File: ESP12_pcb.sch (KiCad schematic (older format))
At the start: 15 parts

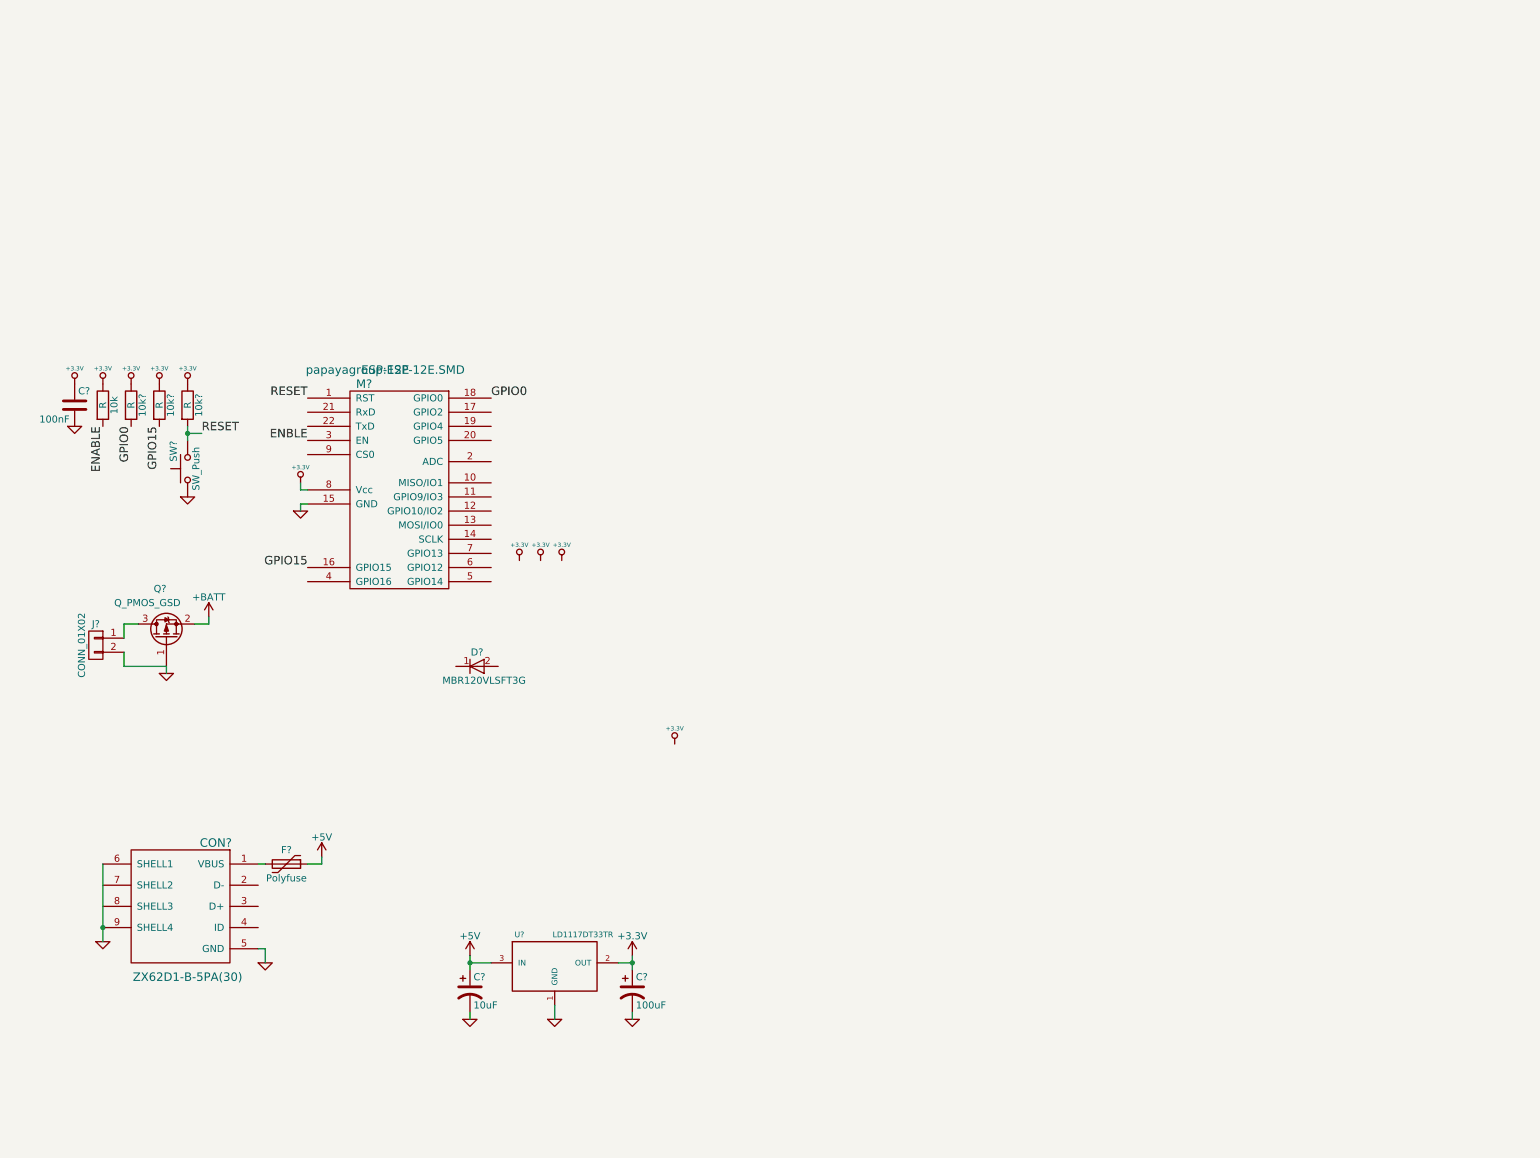
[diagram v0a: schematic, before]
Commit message: Finished power components
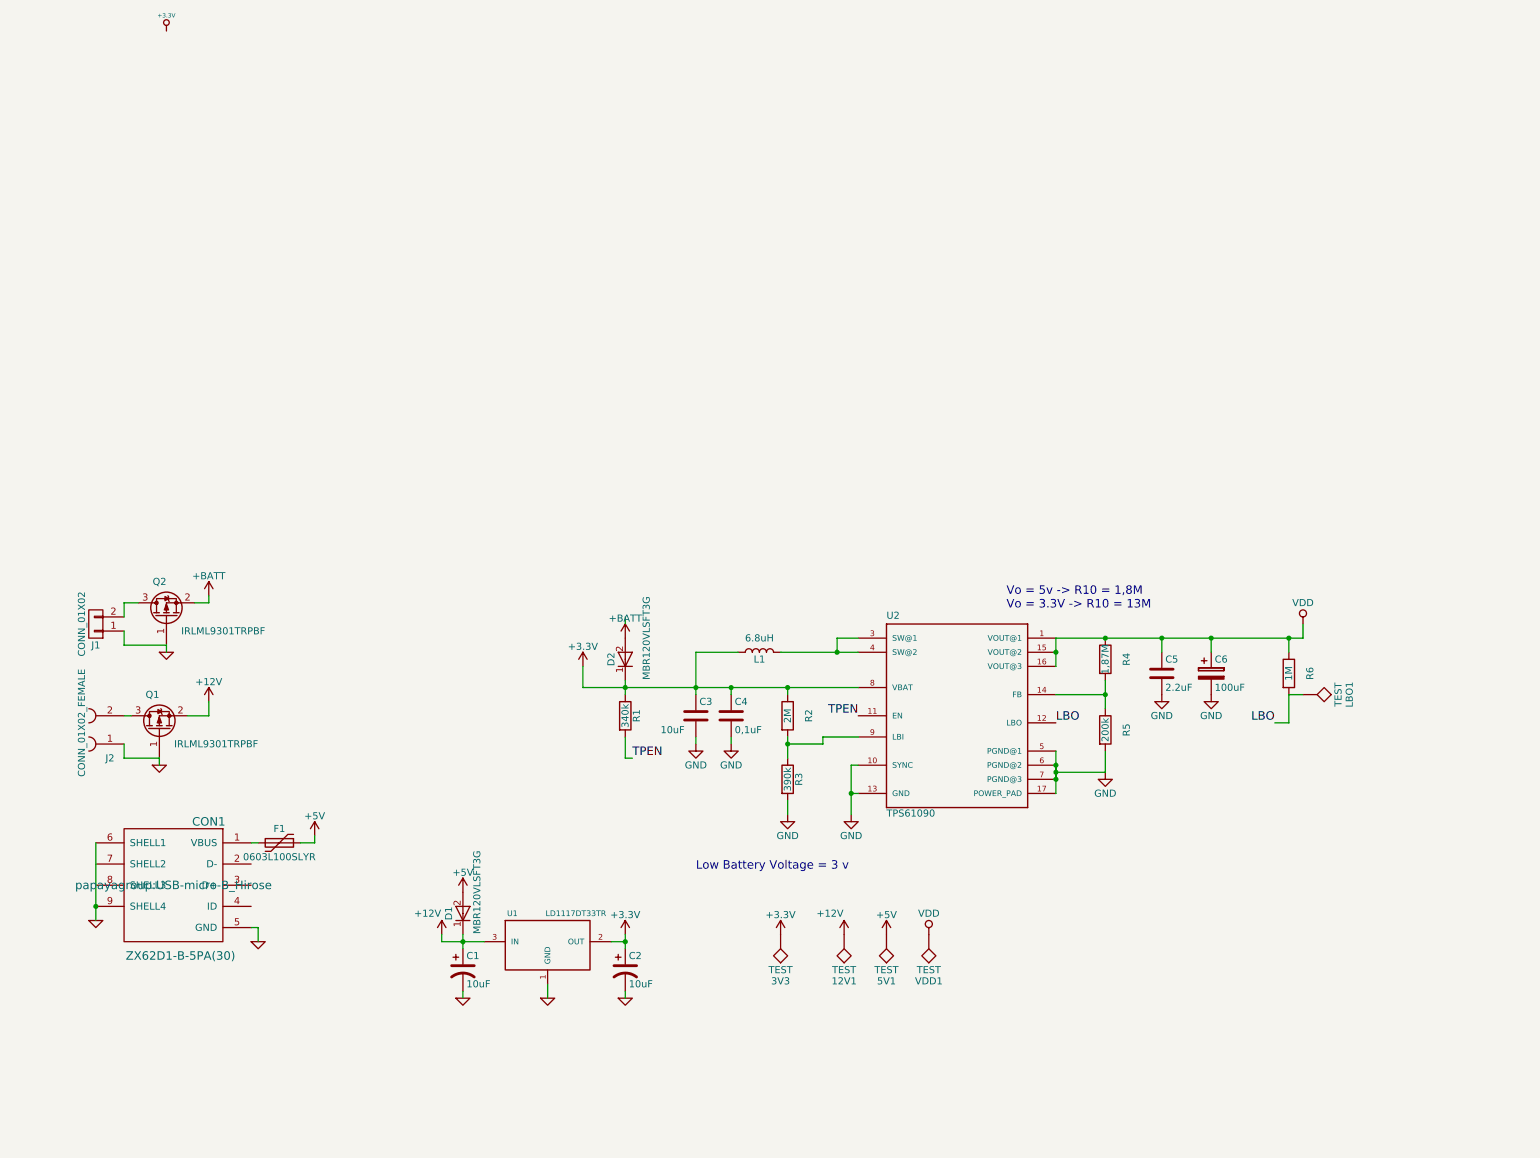
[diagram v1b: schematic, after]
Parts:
- removed 10k, 10k? (x3): R, Resistors_SMD:R_0603_HandSoldering, symbol R
- removed C?: 100nF, Capacitors_SMD:C_0603_HandSoldering, symbol C
- removed C?: 100uF, symbol CP1
- removed M?: ESP-12E, papayagroup:ESP-12E.SMD, symbol ESP-12E
- removed SW?: SW_Push, papayagroup:button_4pin, symbol SW_Push
- added 12V1, 3V3, 5V1, LBO1, VDD1: TEST, Measurement_Points:Measurement_Point_Round-SMD-Pad_Small, symbol TEST
- added C2: 10uF, papayagroup:C_3528, symbol CP1
- added C3: 10uF, Capacitors_SMD:C_0603_HandSoldering, symbol C
- added C4: 0,1uF, Capacitors_SMD:C_0603_HandSoldering, symbol C
- added C5: 2.2uF, Capacitors_SMD:C_0603_HandSoldering, symbol C
- added C6: 100uF, Capacitors_SMD:C_0805_HandSoldering, symbol CP
- added D2: MBR120VLSFT3G, Diodes_SMD:D_SOD-123F, symbol MBR120VLSFT3G
- added J2: CONN_01X02_FEMALE, Connectors:bornier2, symbol CONN_01X02_FEMALE
- added L1: 6.8uH, papayagroup:L_bourns, symbol L
- added Q1: IRLML9301TRPBF, TO_SOT_Packages_SMD:SOT-23, symbol Q_PMOS_GSD
- added R1: 340k, Resistors_SMD:R_0603_HandSoldering, symbol R
- added R2: 2M, Resistors_SMD:R_0603_HandSoldering, symbol R
- added R3: 390k, Resistors_SMD:R_0603_HandSoldering, symbol R
- added R4: 1,87M, Resistors_SMD:R_0603_HandSoldering, symbol R
- added R5: 200k, Resistors_SMD:R_0603_HandSoldering, symbol R
- added R6: 1M, Resistors_SMD:R_0603_HandSoldering, symbol R
- added U2: TPS61090, papayagroup:QFN65P400X400X100-17N, symbol TPS61090
- C1: renamed from C?; footprint (none) -> papayagroup:C_3528
- CON1: renamed from CON?; footprint (none) -> papayagroup:USB-micro-B_Hirose
- D1: renamed from D?; footprint (none) -> Diodes_SMD:D_SOD-123F
- F1: renamed from F?; value Polyfuse -> 0603L100SLYR
- J1: renamed from J?; footprint (none) -> Pin_Headers:Pin_Header_Straight_1x02_Pitch2.54mm
- Q2: renamed from Q?; value Q_PMOS_GSD -> IRLML9301TRPBF
- gave numbers to parts that had none: 1
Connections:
- net +3V3: now also 3V3.1, C2.1, C3.1, C4.1, D2.1 (K), L1.1, R1.1, R2.1, U2.8 (VBAT)
- net +5V: now also D1.2 (A), 5V1.1; no longer C1.1, U1.3 (IN)
- net +BATT: now also D2.2 (A)
- net GND: now also J1.1 (P1), C2.2, C3.2, C4.2, C5.2, C6.2, J2.1, Q1.1 (G), R3.2, R5.2, U2.10 (SYNC), U2.13 (GND), U2.17 (POWER_PAD), U2.5 (PGND@1), U2.6 (PGND@2), U2.7 (PGND@3); no longer J1.2 (P2)
- net at Q2.3 (D): now also J1.2 (P2); no longer J1.1 (P1)
- net +12V: now reaches D1.1 (K)
- net +12V: now also C1.1, U1.3 (IN), 12V1.1, Q1.2 (S)
- new net: J2.2, Q1.3 (D)
- new net: L1.2, U2.3 (SW@1), U2.4 (SW@2)
- new net: R2.2, R3.1, U2.9 (LBI)
- new net: R4.2, R5.1, U2.14 (FB)
- new net LBO: LBO1.1, R6.2, U2.12 (LBO)
- new net TPEN: R1.2, U2.11 (EN)
- new net VDD: C5.1, C6.1, R4.1, R6.1, U2.1 (VOUT@1), U2.15 (VOUT@2), U2.16 (VOUT@3), VDD1.1
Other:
- note added: "Low Battery Voltage = 3 v"
- note added: "Vo = 5v -> R10 = 1,8M\nVo = 3.3V -> R10 = 13M"
- moved on the sheet: C1, CON1, D1, F1, J1, Q2, U1

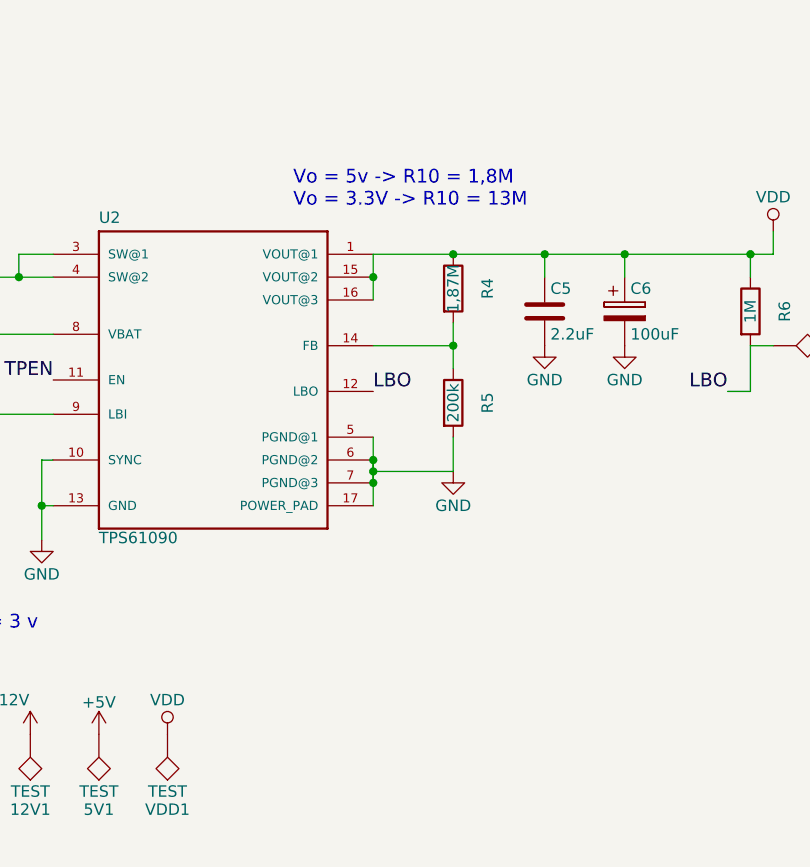
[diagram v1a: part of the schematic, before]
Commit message: Modified Top silk screen
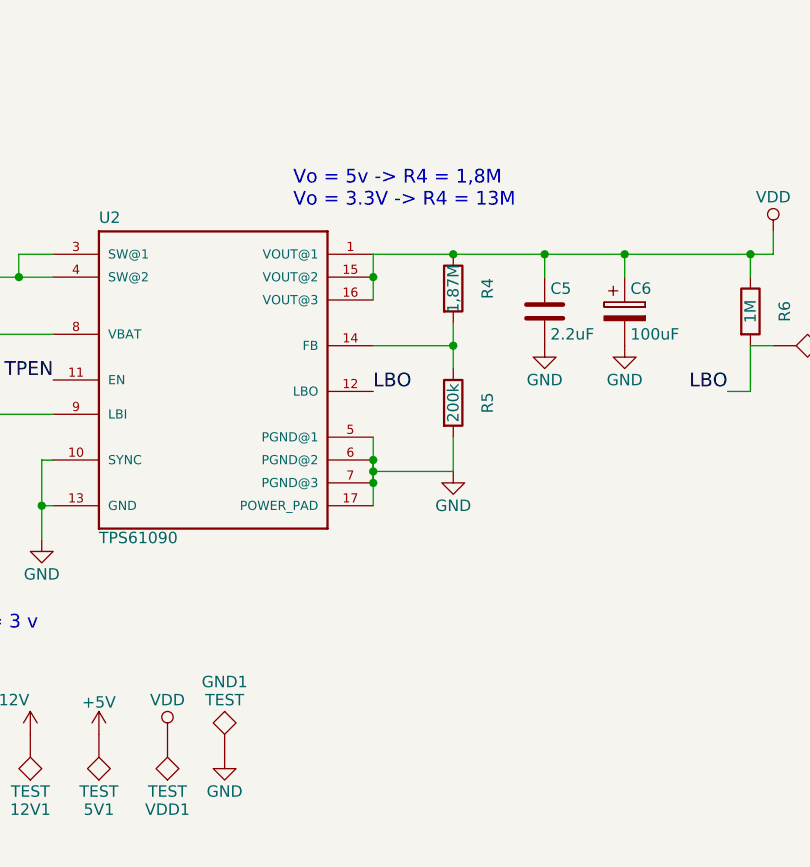
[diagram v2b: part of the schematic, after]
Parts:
- added GND1: TEST, Measurement_Points:Measurement_Point_Round-SMD-Pad_Small, symbol TEST
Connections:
- net GND: now also GND1.1
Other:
- note added: "Vo = 5v -> R4 = 1,8M\nVo = 3.3V -> R4 = 13M"
- note removed: "Vo = 5v -> R10 = 1,8M\nVo = 3.3V -> R10 = 13M"
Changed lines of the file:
@@
 Connection ~ 8950 2750
 Text Notes 7500 2550 0    60   ~ 0
-Vo = 5v -> R10 = 1,8M\nVo = 3.3V -> R10 = 13M
+Vo = 5v -> R4 = 1,8M\nVo = 3.3V -> R4 = 13M
 Text Notes 5300 4400 0    60   ~ 0
 Low Battery Voltage = 3 v
@@
 	0    1    1    0
 $EndComp
+$Comp
+L TEST GND1
+U 1 1 5996B10A
+P 7200 4950
+F 0 "GND1" H 7200 5250 50  0000 C BNN
+F 1 "TEST" H 7200 5200 50  0000 C CNN
+F 2 "Measurement_Points:Measurement_Point_Round-SMD-Pad_Small" H 7200 4950 50  0001 C CNN
+F 3 "" H 7200 4950 50  0001 C CNN
+	1    7200 4950
+	1    0    0    -1
+$EndComp
+$Comp
+L GND #PWR029
+U 1 1 5996B212
+P 7200 4950
+F 0 "#PWR029" H 7200 4700 50  0001 C CNN
+F 1 "GND" H 7200 4800 50  0000 C CNN
+F 2 "" H 7200 4950 50  0000 C CNN
+F 3 "" H 7200 4950 50  0000 C CNN
+	1    7200 4950
+	1    0    0    -1
+$EndComp
 $EndSCHEMATC

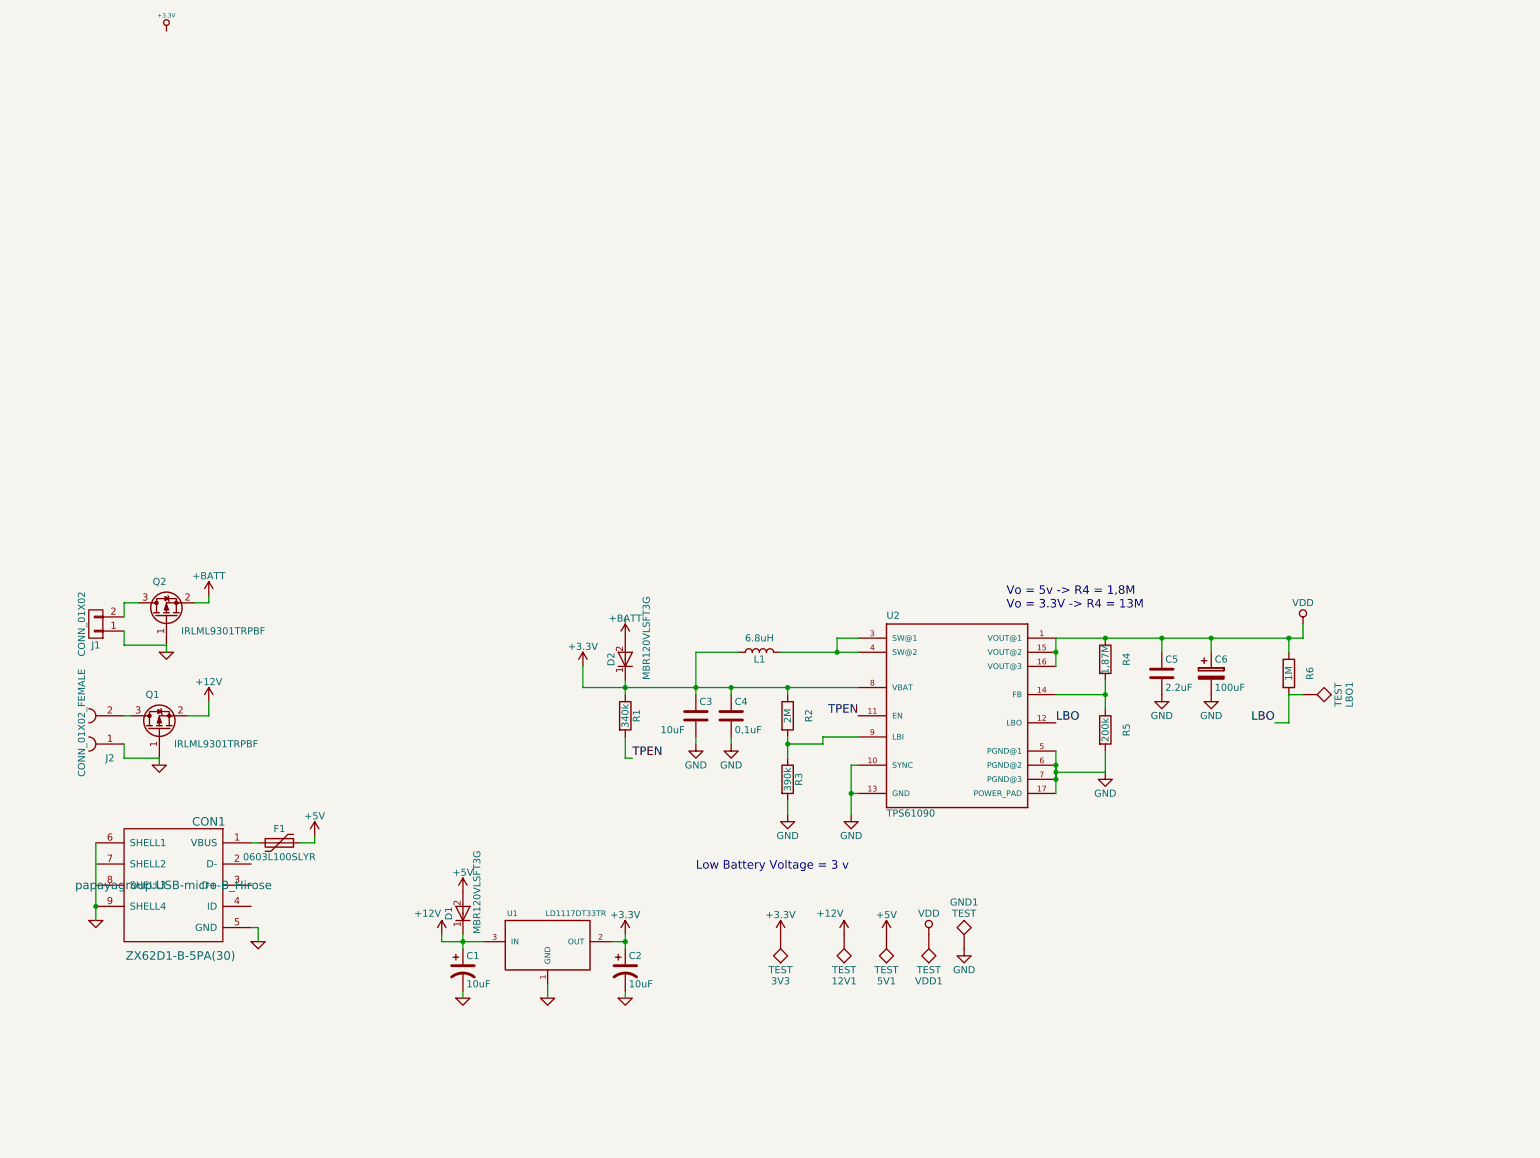
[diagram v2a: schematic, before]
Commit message: Changed one connection for AP2112k
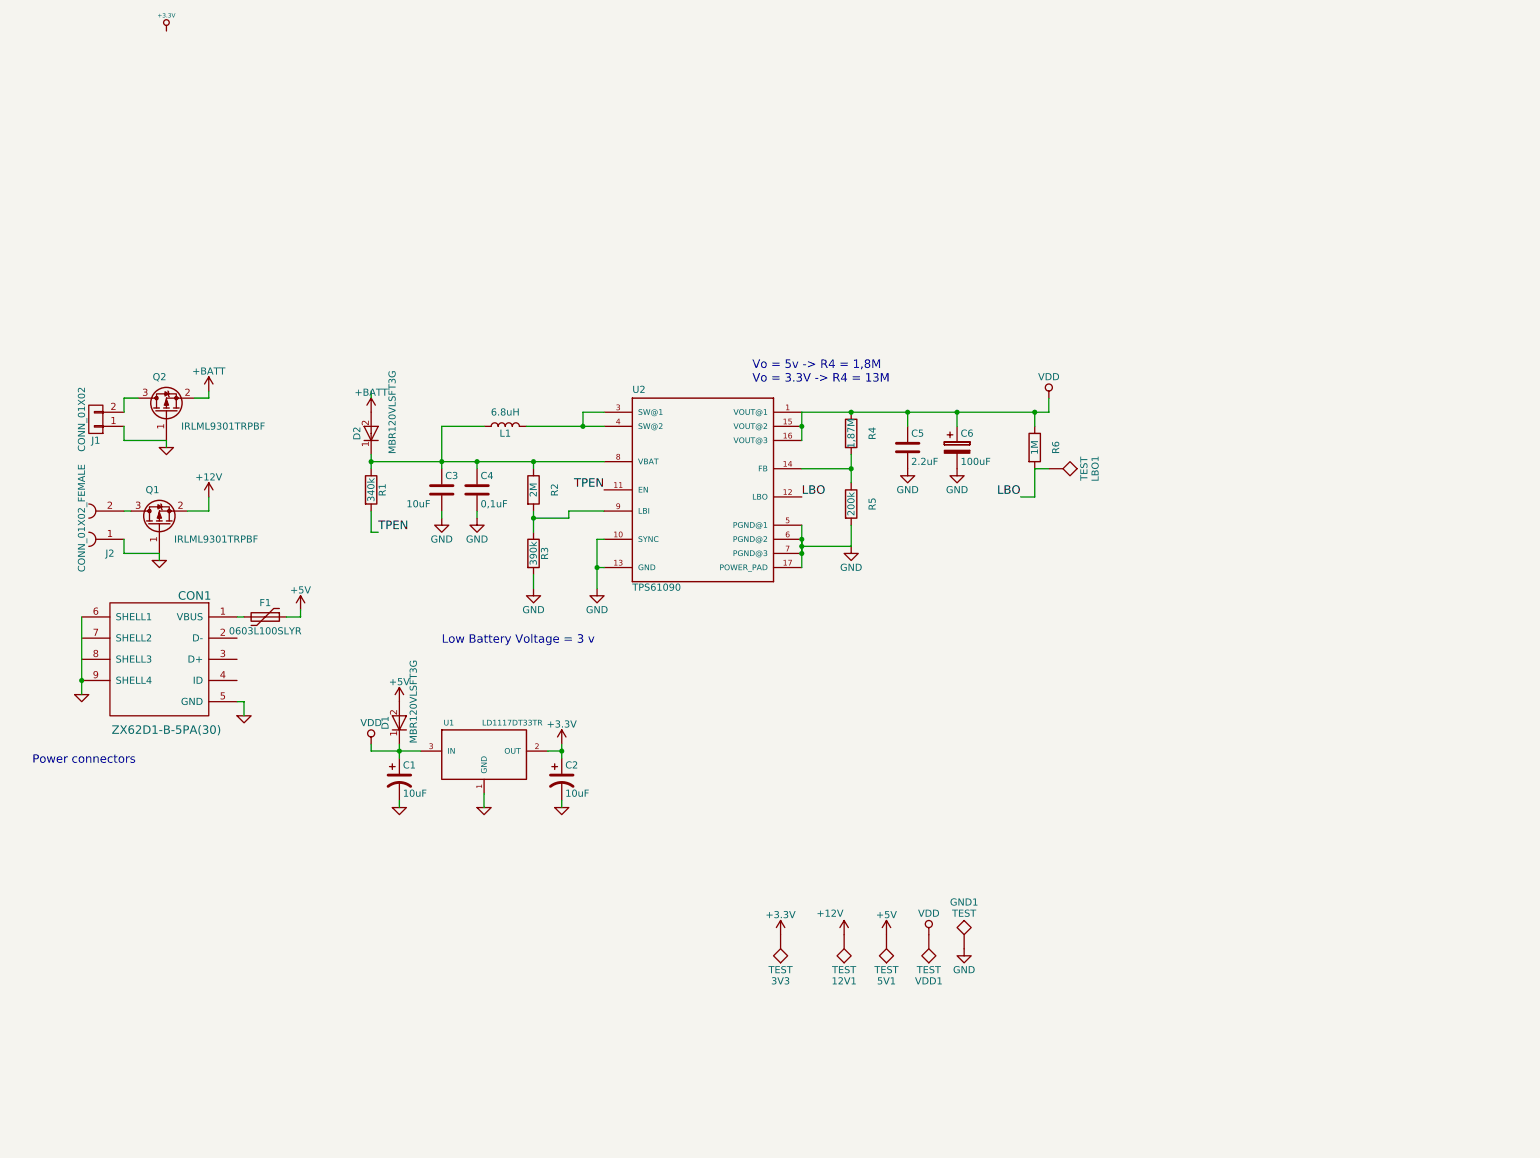
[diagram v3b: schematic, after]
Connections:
- net +12V: no longer C1.1, D1.1 (K), U1.3 (IN)
- net +3V3: no longer C3.1, C4.1, D2.1 (K), L1.1, R1.1, R2.1, U2.8 (VBAT)
- net VDD: now also C1.1, D1.1 (K), U1.3 (IN)
- new net: C3.1, C4.1, D2.1 (K), L1.1, R1.1, R2.1, U2.8 (VBAT)
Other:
- note added: "Power connectors"
- moved on the sheet: C1, C2, C3, C4, C5, C6, CON1, D1, D2, F1, J1, J2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
